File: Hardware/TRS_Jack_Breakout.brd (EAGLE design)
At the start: 27.9 x 15.2 mm, 4 parts

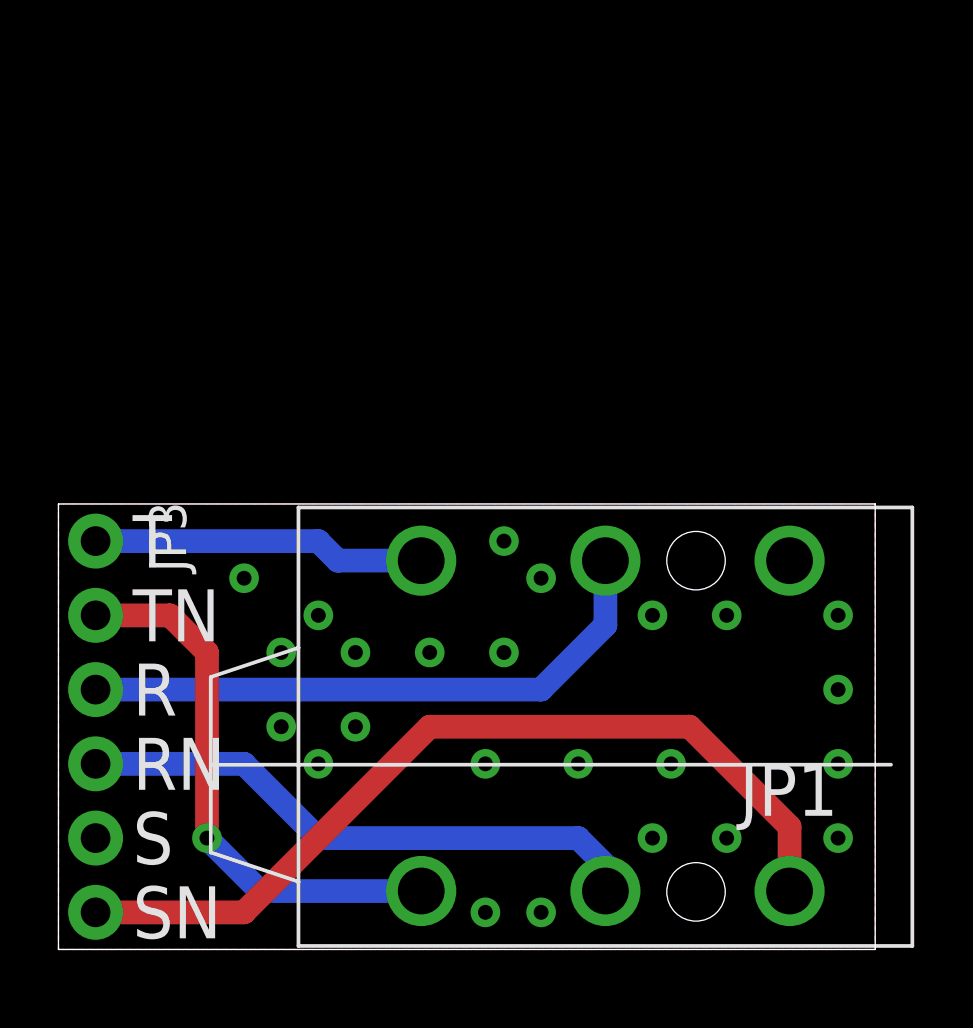
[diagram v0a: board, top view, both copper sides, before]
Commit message: Adding mounting holes on tabls, gnd pin
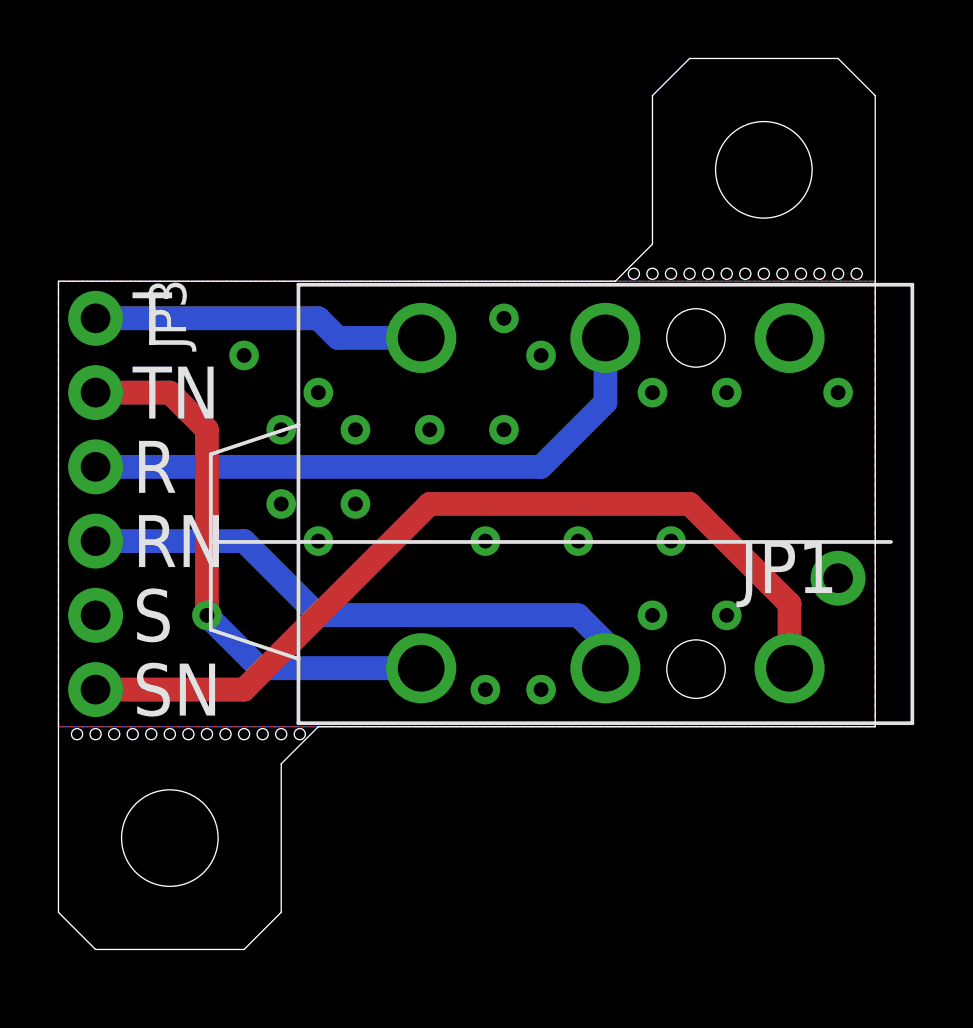
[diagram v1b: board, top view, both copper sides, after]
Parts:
- added JP2: M01SMDNS, SparkFun-Connectors:1X01NS
- added STANDOFF1, STANDOFF2: STAND-OFF, SparkFun-Electromechanical:STAND-OFF
- JP3: value (none) -> HDR
- moved FRAME1 14.2 mm to (7.62, -12.7)
- moved JP1 7.62 mm to (29.2, 14.0)
- moved LOGO1 7.62 mm to (25.4, 14.0)
- moved JP3 7.62 mm to (1.27, 21.6)
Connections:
- net GND: now also JP2.1
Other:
- board size 27.9 x 15.2 mm -> 27.9 x 30.5 mm
- board text added: "Byron Jacquot"
- board text added: "GND"

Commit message: Updating TRS jack footprint
Drawing in datasheet isn't totally correct.  The orientation bosses are
not actually in line with the connections.
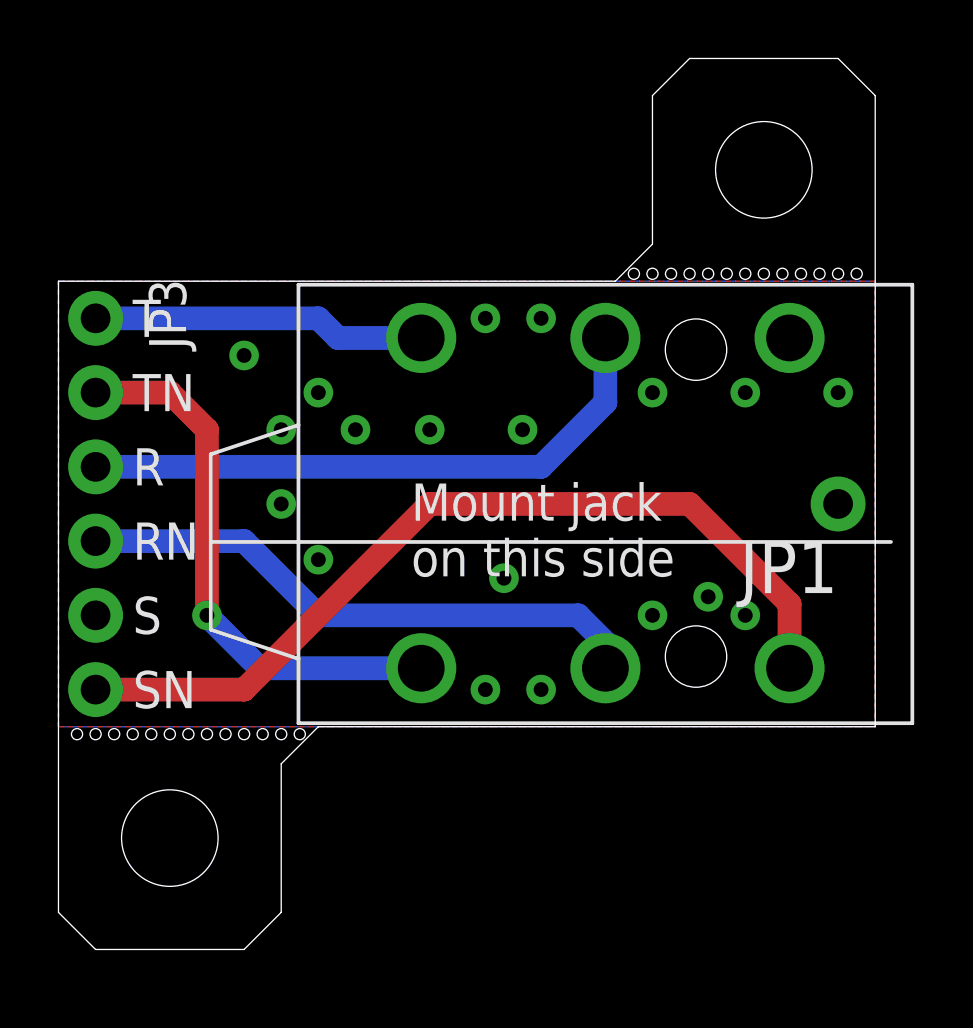
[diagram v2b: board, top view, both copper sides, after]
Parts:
- moved JP2 2.54 mm to (26.7, 15.2)
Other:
- board text added: "Mount jack on this side"
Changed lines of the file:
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@@
 <layer number="27" name="tValues" color="7" fill="1" visible="no" active="yes"/>
 <layer number="28" name="bValues" color="7" fill="1" visible="no" active="yes"/>
-<layer number="29" name="tStop" color="7" fill="3" visible="yes" active="yes"/>
-<layer number="30" name="bStop" color="7" fill="6" visible="yes" active="yes"/>
+<layer number="29" name="tStop" color="7" fill="3" visible="no" active="yes"/>
+<layer number="30" name="bStop" color="7" fill="6" visible="no" active="yes"/>
 <layer number="31" name="tCream" color="7" fill="4" visible="no" active="yes"/>
 <layer number="32" name="bCream" color="7" fill="5" visible="no" active="yes"/>
@@
 <layer number="43" name="vRestrict" color="2" fill="10" visible="no" active="yes"/>
 <layer number="44" name="Drills" color="7" fill="1" visible="no" active="yes"/>
-<layer number="45" name="Holes" color="7" fill="1" visible="yes" active="yes"/>
+<layer number="45" name="Holes" color="7" fill="1" visible="no" active="yes"/>
 <layer number="46" name="Milling" color="3" fill="1" visible="no" active="yes"/>
 <layer number="47" name="Measures" color="7" fill="1" visible="no" active="yes"/>
@@
 <wire x1="8.89" y1="7.62" x2="27.94" y2="7.62" width="0" layer="20"/>
 <wire x1="27.94" y1="7.62" x2="27.94" y2="29.21" width="0" layer="20"/>
-<text x="2.54" y="21.59" size="1.778" layer="21" font="vector" ratio="15" align="center-left">T</text>
-<text x="2.54" y="19.05" size="1.778" layer="21" font="vector" ratio="15" align="center-left">TN</text>
-<text x="2.54" y="16.51" size="1.778" layer="21" font="vector" ratio="15" align="center-left">R</text>
-<text x="2.54" y="13.97" size="1.778" layer="21" font="vector" ratio="15" align="center-left">RN</text>
-<text x="2.54" y="11.43" size="1.778" layer="21" font="vector" ratio="15" align="center-left">S</text>
-<text x="2.54" y="8.89" size="1.778" layer="21" font="vector" ratio="15" align="center-left">SN</text>
+<text x="2.54" y="21.59" size="1.27" layer="21" font="vector" ratio="15" align="center-left">T</text>
+<text x="2.54" y="19.05" size="1.27" layer="21" font="vector" ratio="15" align="center-left">TN</text>
+<text x="2.54" y="16.51" size="1.27" layer="21" font="vector" ratio="15" align="center-left">R</text>
+<text x="2.54" y="13.97" size="1.27" layer="21" font="vector" ratio="15" align="center-left">RN</text>
+<text x="2.54" y="11.43" size="1.27" layer="21" font="vector" ratio="15" align="center-left">S</text>
+<text x="2.54" y="8.89" size="1.27" layer="21" font="vector" ratio="15" align="center-left">SN</text>
 <text x="25.4" y="12.7" size="1.27" layer="22" font="vector" ratio="15" rot="MR0" align="center-left">TRS Jack Breakout</text>
-<text x="26.67" y="13.97" size="1.778" layer="22" font="vector" ratio="15" rot="MR270" align="center-right">GND</text>
-<text x="2.54" y="19.05" size="1.778" layer="22" font="vector" ratio="15" rot="MR0" align="center-right">TN</text>
-<text x="2.54" y="16.51" size="1.778" layer="22" font="vector" ratio="15" rot="MR0" align="center-right">R</text>
-<text x="2.54" y="13.97" size="1.778" layer="22" font="vector" ratio="15" rot="MR0" align="center-right">RN</text>
-<text x="2.54" y="11.43" size="1.778" layer="22" font="vector" ratio="15" rot="MR0" align="center-right">S</text>
-<text x="2.54" y="8.89" size="1.778" layer="22" font="vector" ratio="15" rot="MR0" align="center-right">SN</text>
+<text x="26.67" y="13.97" size="1.27" layer="22" font="vector" ratio="15" rot="MR90" align="center-right">GND</text>
+<text x="2.54" y="19.05" size="1.27" layer="22" font="vector" ratio="15" rot="MR0" align="center-right">TN</text>
+<text x="2.54" y="16.51" size="1.27" layer="22" font="vector" ratio="15" rot="MR0" align="center-right">R</text>
+<text x="2.54" y="13.97" size="1.27" layer="22" font="vector" ratio="15" rot="MR0" align="center-right">RN</text>
+<text x="2.54" y="11.43" size="1.27" layer="22" font="vector" ratio="15" rot="MR0" align="center-right">S</text>
+<text x="2.54" y="8.89" size="1.27" layer="22" font="vector" ratio="15" rot="MR0" align="center-right">SN</text>
 <text x="34.29" y="-12.7" size="1.778" layer="51" font="vector" ratio="15">Byron Jacquot</text>
 <hole x="1.905" y="7.366" drill="0.381"/>
@@
 <hole x="25.4" y="23.114" drill="0.381"/>
 <hole x="26.67" y="23.114" drill="0.381"/>
+<text x="2.54" y="21.59" size="1.27" layer="22" font="vector" ratio="15" rot="MR0" align="center-right">T</text>
+<text x="12.065" y="14.351" size="1.27" layer="21" font="vector" ratio="15" align="center-left">Mount jack
+on this side</text>
 </plain>
 <attributes>
@@
 <element name="STANDOFF1" library="SparkFun-Electromechanical" package="STAND-OFF" value="STAND-OFF" x="24.13" y="26.67"/>
 <element name="STANDOFF2" library="SparkFun-Electromechanical" package="STAND-OFF" value="STAND-OFF" x="3.81" y="3.81"/>
-<element name="JP2" library="SparkFun-Connectors" package="1X01NS" value="M01SMDNS" x="26.67" y="12.7"/>
+<element name="JP2" library="SparkFun-Connectors" package="1X01NS" value="M01SMDNS" x="26.67" y="15.24"/>
 </elements>
 <signals>
@@
 <vertex x="0" y="7.62"/>
 </polygon>
-<via x="16.51" y="20.32" extent="1-16" drill="0.508"/>
-<via x="15.24" y="17.78" extent="1-16" drill="0.508"/>
+<via x="16.51" y="21.59" extent="1-16" drill="0.508"/>
+<via x="15.875" y="17.78" extent="1-16" drill="0.508"/>
 <via x="12.7" y="17.78" extent="1-16" drill="0.508"/>
 <via x="10.16" y="17.78" extent="1-16" drill="0.508"/>
@@
 <via x="6.35" y="20.32" extent="1-16" drill="0.508"/>
 <via x="8.89" y="19.05" extent="1-16" drill="0.508"/>
-<via x="15.24" y="21.59" extent="1-16" drill="0.508"/>
-<via x="17.78" y="13.97" extent="1-16" drill="0.508"/>
+<via x="14.605" y="21.59" extent="1-16" drill="0.508"/>
 <via x="20.32" y="11.43" extent="1-16" drill="0.508"/>
 <via x="16.51" y="8.89" extent="1-16" drill="0.508"/>
 <via x="14.605" y="8.89" extent="1-16" drill="0.508"/>
-<via x="14.605" y="13.97" extent="1-16" drill="0.508"/>
-<via x="20.955" y="13.97" extent="1-16" drill="0.508"/>
-<via x="22.86" y="11.43" extent="1-16" drill="0.508"/>
-<via x="10.16" y="15.24" extent="1-16" drill="0.508"/>
-<via x="8.89" y="13.97" extent="1-16" drill="0.508"/>
+<via x="15.24" y="12.7" extent="1-16" drill="0.508"/>
+<via x="22.225" y="12.065" extent="1-16" drill="0.508"/>
+<via x="23.495" y="11.43" extent="1-16" drill="0.508"/>
+<via x="8.89" y="13.335" extent="1-16" drill="0.508"/>
 <via x="7.62" y="15.24" extent="1-16" drill="0.508"/>
 <via x="26.67" y="19.05" extent="1-16" drill="0.508"/>
-<via x="22.86" y="19.05" extent="1-16" drill="0.508"/>
+<via x="23.495" y="19.05" extent="1-16" drill="0.508"/>
 <via x="20.32" y="19.05" extent="1-16" drill="0.508"/>
 <contactref element="JP2" pad="1"/>
@@
 </board>
 </drawing>
+<compatibility>
+<note version="6.3" minversion="6.2.2" severity="warning">
+Since Version 6.2.2 text objects can contain more than one line,
+which will not be processed correctly with this version.
+</note>
+</compatibility>
 </eagle>

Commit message: Updating footprint based on protos
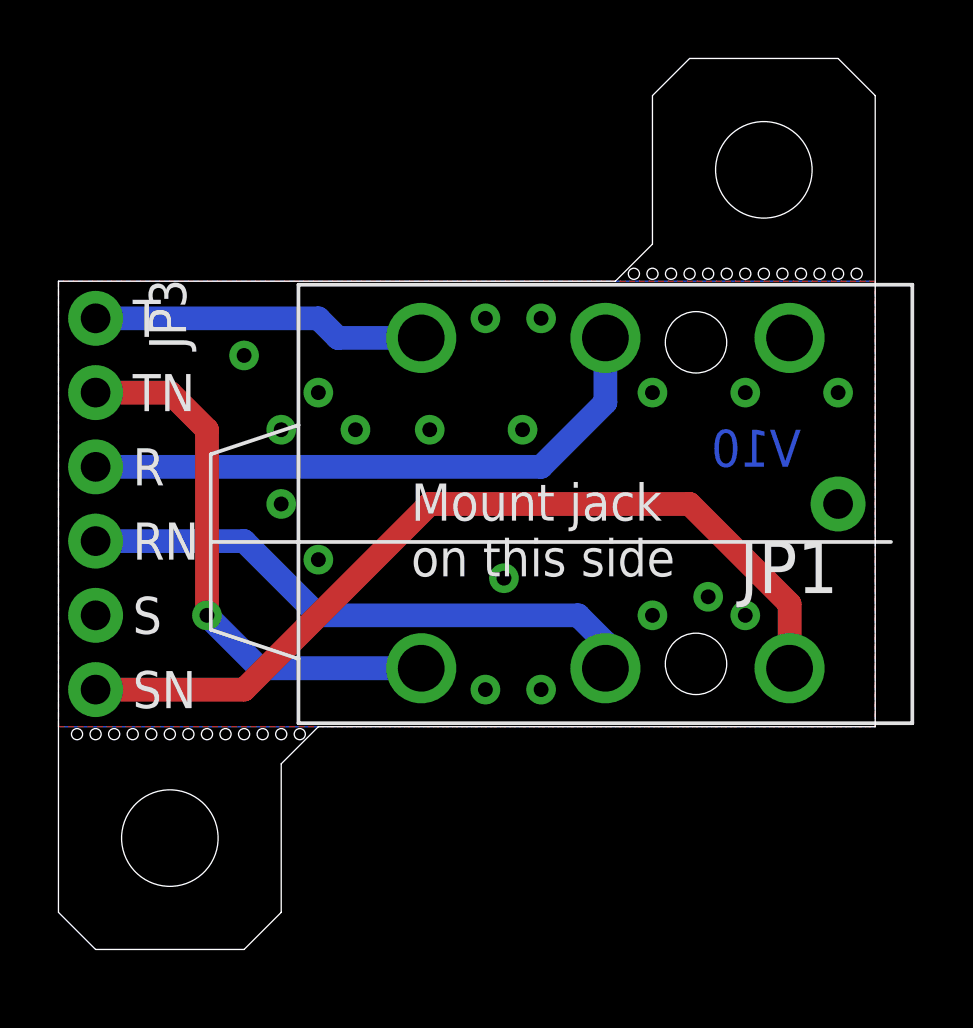
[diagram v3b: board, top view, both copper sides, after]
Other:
- board text added: "V10"
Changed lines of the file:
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@@
 <layer number="43" name="vRestrict" color="2" fill="10" visible="no" active="yes"/>
 <layer number="44" name="Drills" color="7" fill="1" visible="no" active="yes"/>
-<layer number="45" name="Holes" color="7" fill="1" visible="no" active="yes"/>
+<layer number="45" name="Holes" color="7" fill="1" visible="yes" active="yes"/>
 <layer number="46" name="Milling" color="3" fill="1" visible="no" active="yes"/>
 <layer number="47" name="Measures" color="7" fill="1" visible="no" active="yes"/>
@@
 <text x="12.065" y="14.351" size="1.27" layer="21" font="vector" ratio="15" align="center-left">Mount jack
 on this side</text>
+<text x="25.4" y="16.51" size="1.27" layer="16" font="vector" ratio="15" rot="MR0">V10</text>
 </plain>
 <attributes>
